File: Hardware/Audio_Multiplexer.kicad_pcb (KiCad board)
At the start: 2 copper layers, 147 x 40 mm, 14 parts, among them J1 FC68131, J2 FC68131, J3 FC68131, J4 FC68131, J5 FC68131, J6 FC68131, J7 FC68131, SW1 7301SYZQE, SW2 7301SYZQE, SW3 7301SYZQE

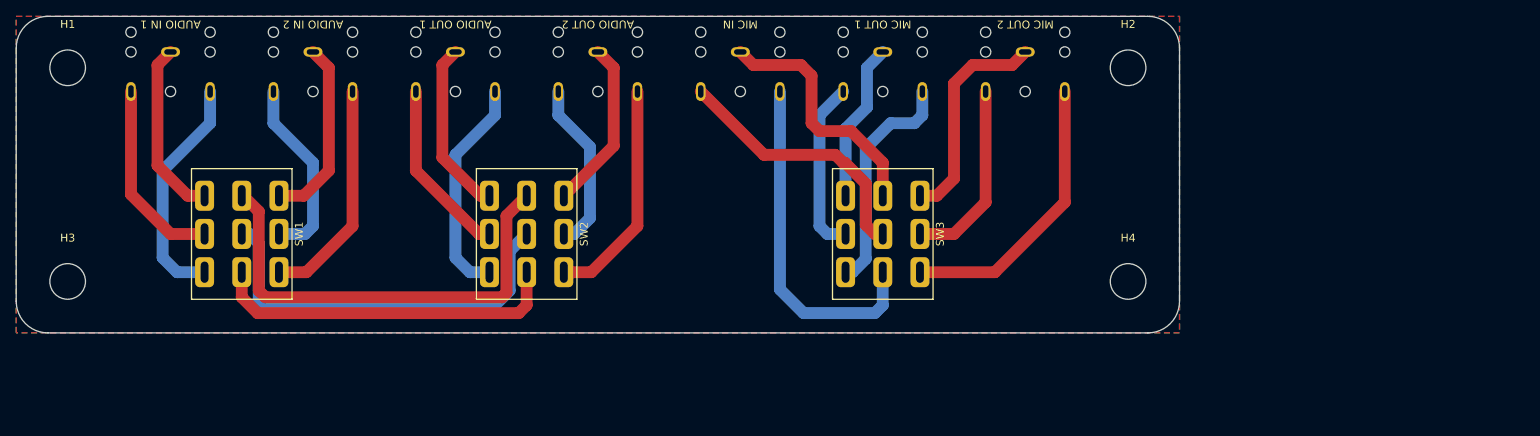
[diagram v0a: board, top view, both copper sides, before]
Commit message: Decreased PCB width by one millimeter so the casing can be 2 millimeters large on each side.
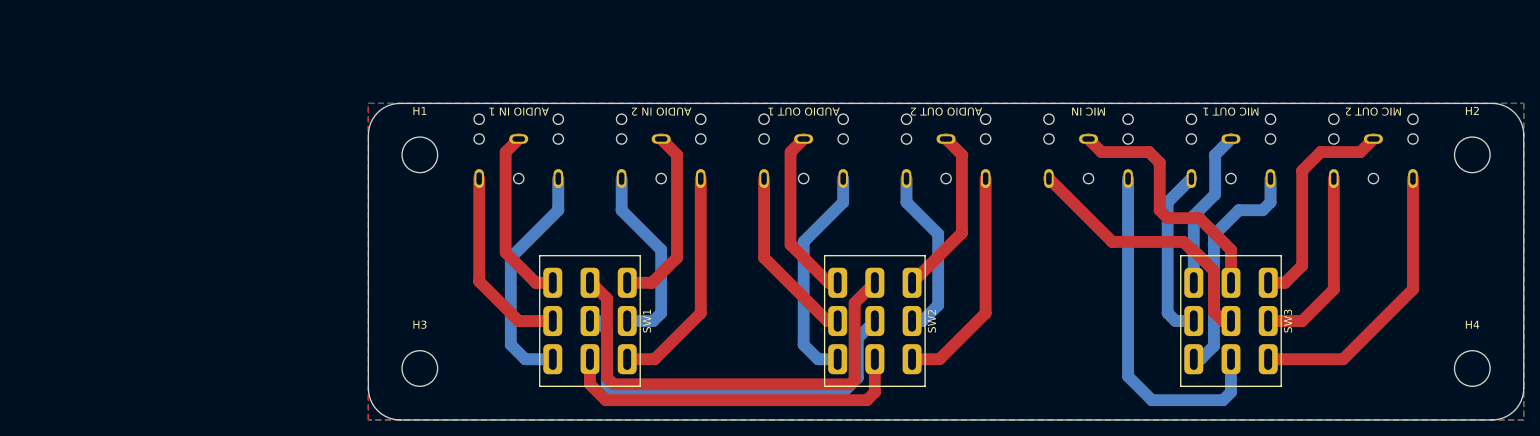
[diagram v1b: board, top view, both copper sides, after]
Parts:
- moved H1 45.8 mm to (83.5, 81.0)
- moved H3 45.8 mm to (83.5, 108.0)
- moved J1 45.4 mm to (96.0, 79.0)
- moved J2 45.4 mm to (114.0, 79.0)
- moved J3 45.4 mm to (132.0, 79.0)
- moved J4 45.4 mm to (150.0, 79.0)
- moved J5 45.4 mm to (168.0, 79.0)
- moved J6 45.4 mm to (186.0, 79.0)
- moved J7 45.4 mm to (204.0, 79.0)
- moved SW1 45.4 mm to (105.0, 102.0)
- moved SW2 45.4 mm to (141.0, 102.0)
- moved SW3 45.4 mm to (186.0, 102.0)
- moved H2 44.9 mm to (216.5, 81.0)
- moved H4 44.9 mm to (216.5, 108.0)
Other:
- board size 147 x 40 mm -> 146 x 40 mm
